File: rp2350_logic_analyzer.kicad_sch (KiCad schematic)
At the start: 35 parts, among them J1 Conn_02x04, J2 Conn_01x03, J3 Conn_01x03, J4 Conn_01x03, J5 Conn_01x03, U1 ISO7761FDBQ, U2 TLV3501AIDBV, U3 TLV3501AIDBV, U4 TLV3501AIDBV, U5 TLV3501AIDBV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

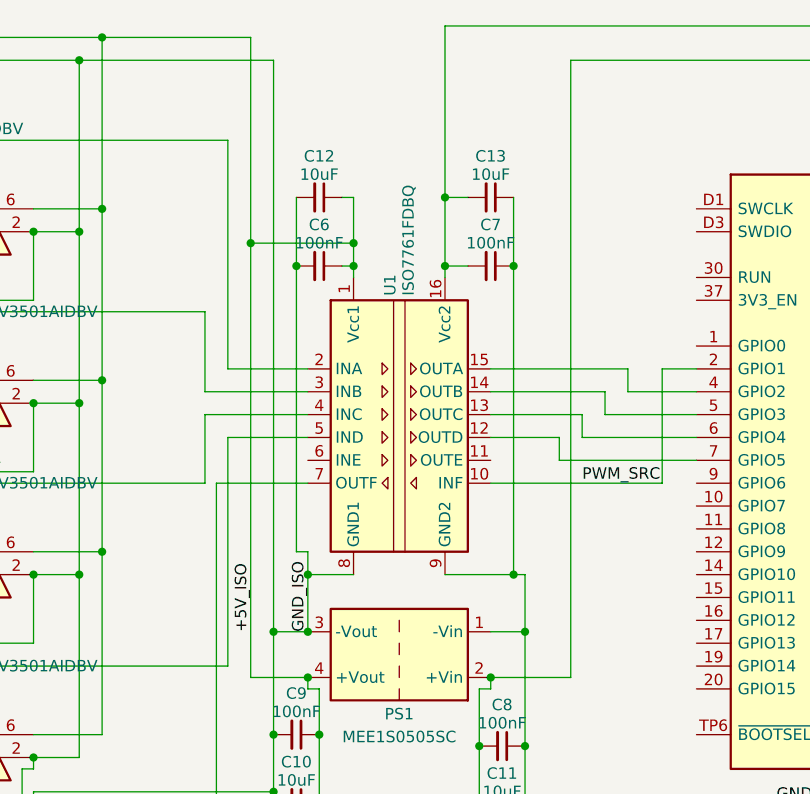
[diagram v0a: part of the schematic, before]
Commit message: Replace ISO7761FDBQ with SI8661BD-B-IS
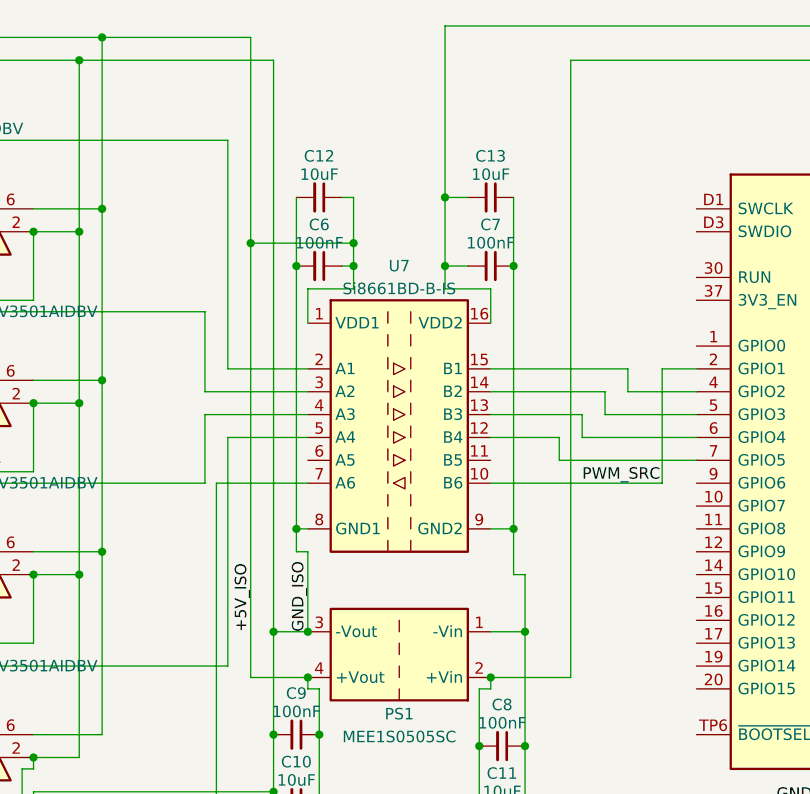
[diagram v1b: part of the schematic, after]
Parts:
- removed U1: ISO7761FDBQ, Package_SO:SSOP-16_3.9x4.9mm_P0.635mm, symbol Isolator:ISO7761FDBQ
- added U7: Si8661BD-B-IS, Package_SO:SOIC-16W_7.5x10.3mm_P1.27mm, symbol Isolator:Si8661BD-B-IS
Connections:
- net +3V3: now also U7.16 (VDD2)
- net +5V_ISO: now also U7.1 (VDD1)
- net GND: now also U7.9 (GND2)
- net GND_ISO: now also U7.8 (GND1)
- net PWM_FROM_ISO: now also U7.7 (A6)
- net PWM_SRC: now also U7.10 (B6)
- net at A1.7 (GPIO5): now also U7.12 (B4)
- net at A1.6 (GPIO4): now also U7.13 (B3)
- net at A1.5 (GPIO3): now also U7.14 (B2)
- net at A1.4 (GPIO2): now also U7.15 (B1)
- net at U2.5: now also U7.2 (A1)
- net at U3.5: now also U7.3 (A2)
- net at U4.5: now also U7.4 (A3)
- net at U5.5: now also U7.5 (A4)
